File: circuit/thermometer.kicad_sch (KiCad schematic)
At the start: 1 part, among them IC1 ICL7107CPL

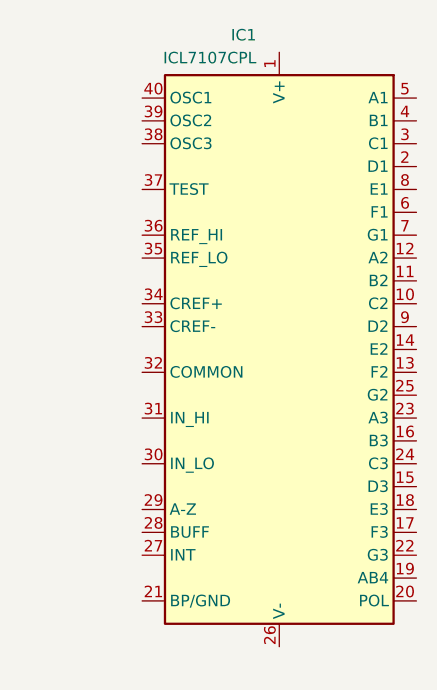
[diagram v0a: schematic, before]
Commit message: Configure oscillator
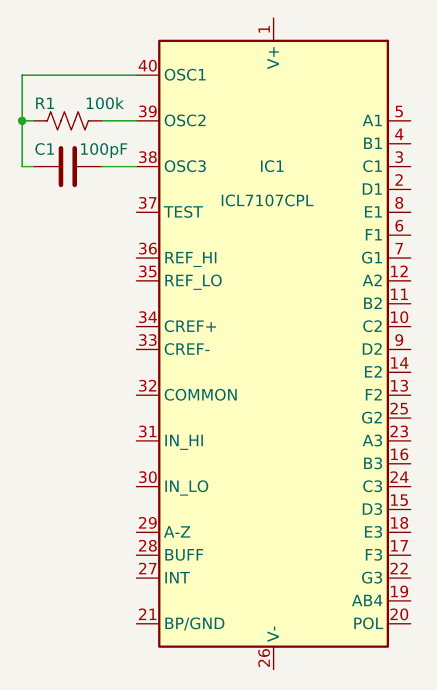
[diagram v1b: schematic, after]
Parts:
- added C1: 100pF, Capacitor_THT:C_Disc_D4.3mm_W1.9mm_P5.00mm, symbol Device:C
- added R1: 100k, Resistor_THT:R_Axial_DIN0207_L6.3mm_D2.5mm_P7.62mm_Horizontal, symbol Device:R_US
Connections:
- net at IC1.38 (OSC3): now also C1.1
- net at IC1.39 (OSC2): now also R1.1
- net at IC1.40 (OSC1): now also C1.2, R1.2
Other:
- moved on the sheet: IC1
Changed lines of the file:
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@@
 (kicad_sch (version 20230121) (generator eeschema)
   (paper "A4")
-  (symbol (lib_id "Analog_ADC:ICL7107CPL") (at 100.965 93.98 0) (mirror y) (unit 1)
+  (junction (at 72.39 68.58) (diameter 0) (color 0 0 0 0)
+  )
+  (wire (pts (xy 72.39 73.66) (xy 72.39 68.58))
+    (stroke (width 0) (type default))
+  )
+  (wire (pts (xy 72.39 68.58) (xy 72.39 63.5))
+    (stroke (width 0) (type default))
+  )
+  (wire (pts (xy 72.39 68.58) (xy 73.66 68.58))
+    (stroke (width 0) (type default))
+  )
+  (wire (pts (xy 72.39 63.5) (xy 85.09 63.5))
+    (stroke (width 0) (type default))
+  )
+  (wire (pts (xy 81.28 68.58) (xy 85.09 68.58))
+    (stroke (width 0) (type default))
+  )
+  (wire (pts (xy 81.28 73.66) (xy 85.09 73.66))
+    (stroke (width 0) (type default))
+  )
+  (wire (pts (xy 72.39 73.66) (xy 73.66 73.66))
+    (stroke (width 0) (type default))
+  )
+  (symbol (lib_id "Analog_ADC:ICL7107CPL") (at 100.33 96.52 0) (mirror y) (unit 1)
     (in_bom yes) (on_board yes) (dnp no)
-    (property "Reference" "IC1" (at 98.4232 59.055 0)
+    (property "Reference" "IC1" (at 101.6 73.66 0)
       (effects (font (size 1.27 1.27)) (justify left))
     )
-    (property "Value" "ICL7107CPL" (at 98.4232 61.595 0)
+    (property "Value" "ICL7107CPL" (at 104.775 77.47 0)
       (effects (font (size 1.27 1.27)) (justify left))
     )
-    (property "Footprint" "Package_DIP:DIP-40_W15.24mm" (at 100.965 125.73 0)
+    (property "Footprint" "Package_DIP:DIP-40_W15.24mm" (at 100.33 128.27 0)
       (effects (font (size 1.27 1.27)) hide)
     )
-    (property "Datasheet" "https://www.renesas.com/eu/en/www/doc/datasheet/icl7106-07-07s.pdf" (at 100.965 92.71 0)
+    (property "Datasheet" "https://www.renesas.com/eu/en/www/doc/datasheet/icl7106-07-07s.pdf" (at 100.33 95.25 0)
       (effects (font (size 1.27 1.27)) hide)
     )
@@
         )
       )
+    )
+  )
+  (symbol (lib_id "Device:R_US") (at 77.47 68.58 270) (unit 1)
+    (in_bom yes) (on_board yes) (dnp no)
+    (property "Reference" "R1" (at 74.93 66.675 90)
+      (effects (font (size 1.27 1.27)))
+    )
+    (property "Value" "100k" (at 79.375 66.675 90)
+      (effects (font (size 1.27 1.27)) (justify left))
+    )
+    (property "Footprint" "Resistor_THT:R_Axial_DIN0207_L6.3mm_D2.5mm_P7.62mm_Horizontal" (at 77.216 69.596 90)
+      (effects (font (size 1.27 1.27)) hide)
+    )
+    (property "Datasheet" "~" (at 77.47 68.58 0)
+      (effects (font (size 1.27 1.27)) hide)
+    )
+    (pin "1")
+    (pin "2")
+    (instances
+      (project "thermometer"
+        (path "/3d49da3f-611f-4a55-80ff-dd730f896849"
+          (reference "R1") (unit 1)
+        )
+      )
+    )
+  )
+  (symbol (lib_id "Device:C") (at 77.47 73.66 270) (unit 1)
+    (in_bom yes) (on_board yes) (dnp no)
+    (property "Reference" "C1" (at 74.93 71.755 90)
+      (effects (font (size 1.27 1.27)))
+    )
+    (property "Value" "100pF" (at 78.74 71.755 90)
+      (effects (font (size 1.27 1.27)) (justify left))
+    )
+    (property "Footprint" "Capacitor_THT:C_Disc_D4.3mm_W1.9mm_P5.00mm" (at 73.66 74.6252 0)
+      (effects (font (size 1.27 1.27)) hide)
+    )
+    (property "Datasheet" "~" (at 77.47 73.66 0)
+      (effects (font (size 1.27 1.27)) hide)
+    )
+    (pin "1")
+    (pin "2")
+    (instances
+      (project "thermometer"
+        (path "/3d49da3f-611f-4a55-80ff-dd730f896849"
+          (reference "C1") (unit 1)
+        )
+      )

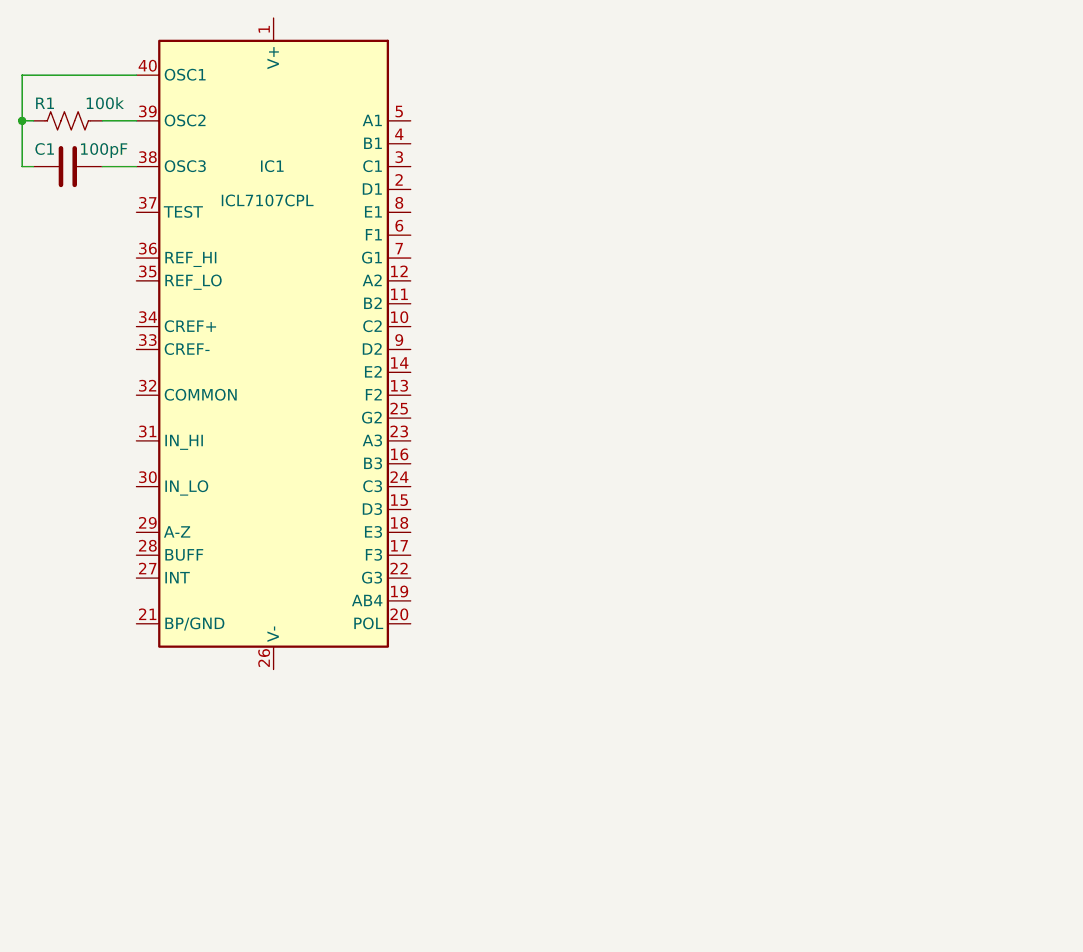
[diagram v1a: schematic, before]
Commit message: Add supporting components and power inverter
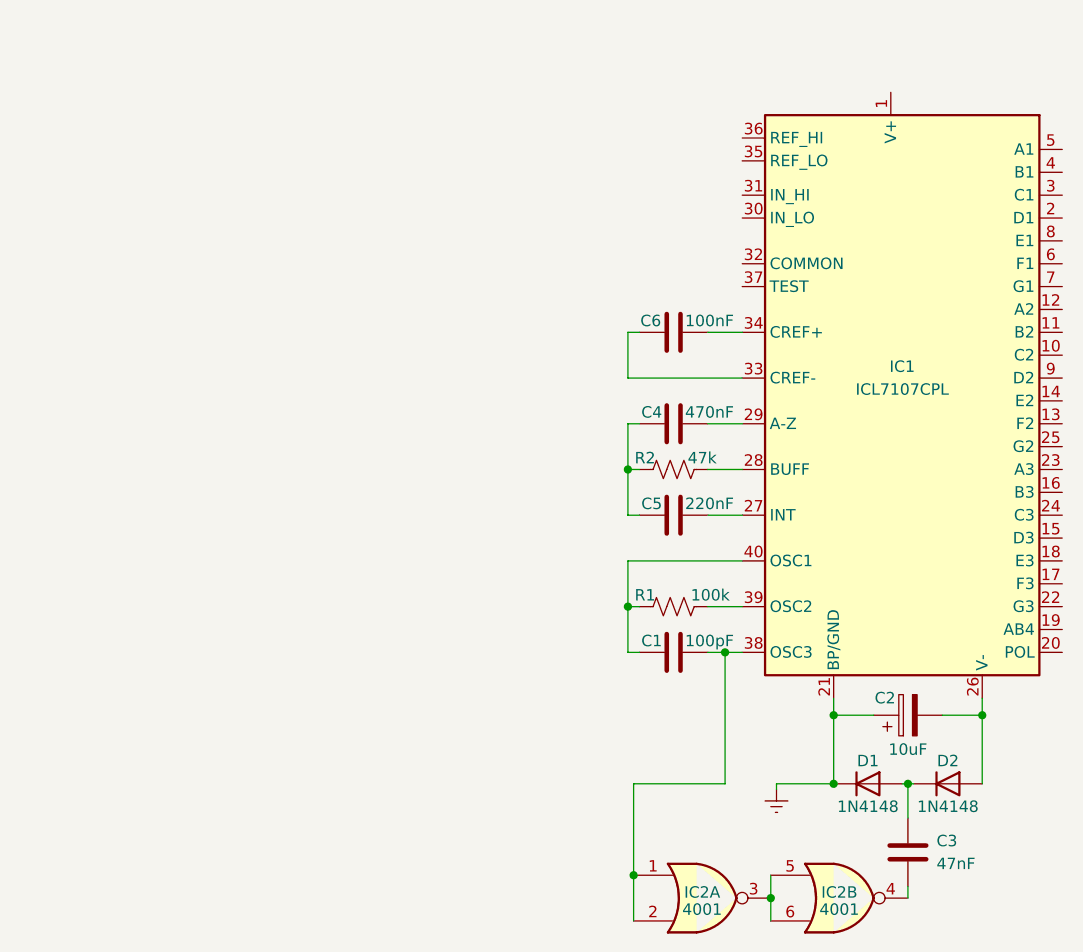
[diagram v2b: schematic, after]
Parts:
- added C2: 10uF, Capacitor_THT:CP_Radial_D5.0mm_P2.50mm, symbol Device:C_Polarized
- added C3: 47nF, Capacitor_THT:C_Disc_D4.3mm_W1.9mm_P5.00mm, symbol Device:C
- added C4: 470nF, Capacitor_THT:C_Disc_D4.3mm_W1.9mm_P5.00mm, symbol Device:C
- added C5: 220nF, Capacitor_THT:C_Disc_D4.3mm_W1.9mm_P5.00mm, symbol Device:C
- added C6: 100nF, symbol Device:C
- added D1, D2: 1N4148, Diode_THT:D_A-405_P7.62mm_Horizontal, symbol Device:D
- added IC2: 4001, Package_DIP:DIP-14_W7.62mm_Socket_LongPads, symbol 4xxx:4001
- added R2: 47k, Resistor_THT:R_Axial_DIN0207_L6.3mm_D2.5mm_P7.62mm_Horizontal, symbol Device:R_US
- IC1: footprint Package_DIP:DIP-40_W15.24mm -> Package_DIP:DIP-40_W15.24mm_Socket_LongPads
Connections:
- net Earth: now reaches IC1.21 (BP/GND)
- net Earth: now also C2.1, D1.1 (K)
- net at IC1.26 (V-): now also C2.2, D2.2 (A)
- net at IC1.27 (INT): now also C5.2
- net at IC1.28 (BUFF): now also R2.1
- net at IC1.29 (A-Z): now also C4.2
- net at IC1.33 (CREF-): now also C6.1
- net at IC1.34 (CREF+): now also C6.2
- net at C1.1, IC1.38 (OSC3): now also IC2.1, IC2.2
- new net: C4.1, C5.1, R2.2
- new net: C3.1, D1.2 (A), D2.1 (K)
- new net: C3.2, IC2.4
- new net: IC2.3, IC2.5, IC2.6
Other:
- moved on the sheet: C1, IC1, R1

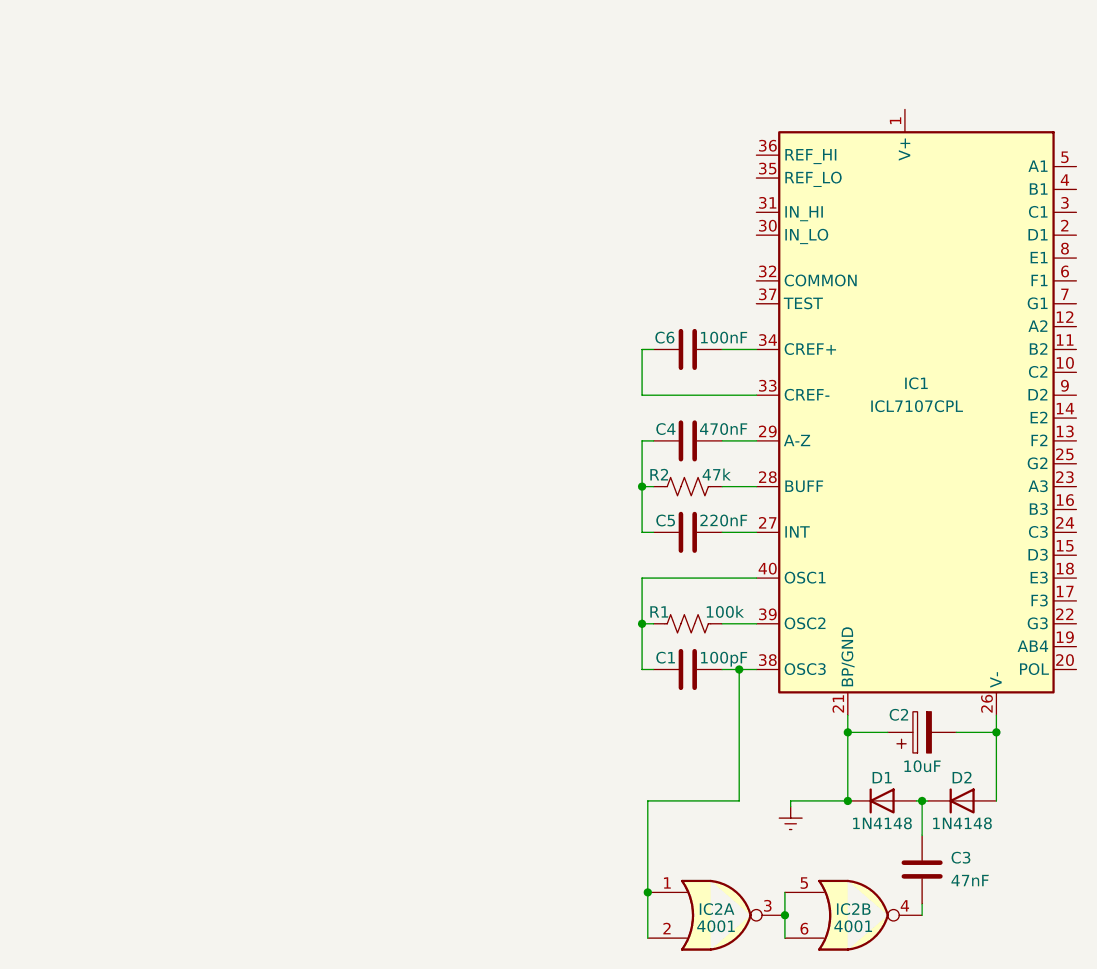
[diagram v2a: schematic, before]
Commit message: Place all remaining thermometer parts
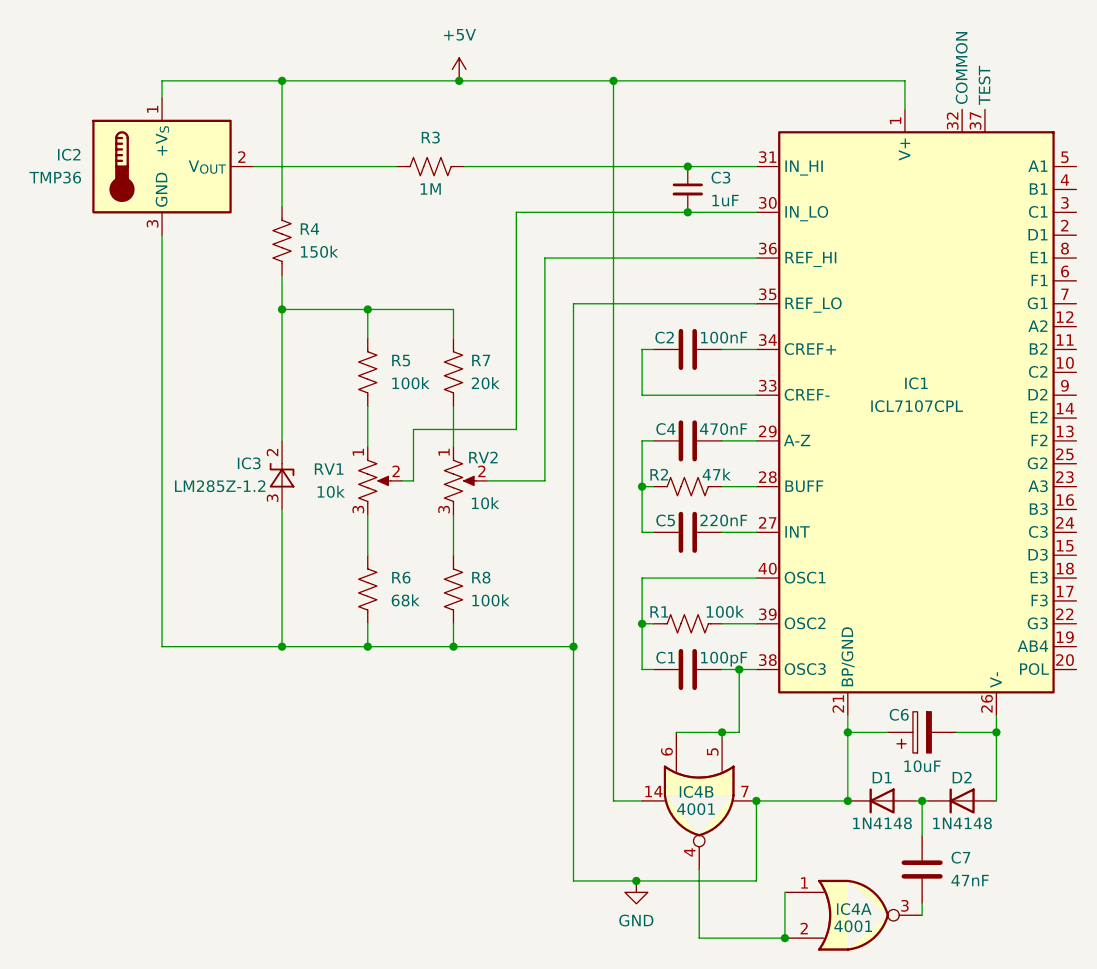
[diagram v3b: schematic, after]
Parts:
- added C3: 1uF, Capacitor_THT:C_Disc_D4.3mm_W1.9mm_P5.00mm, symbol Device:C_Small
- added IC2: TMP36, Package_TO_SOT_THT:TO-92_Inline, symbol Sensor_Temperature:LM35-LP
- added IC3: LM285Z-1.2, Package_TO_SOT_THT:TO-92_Inline, symbol Reference_Voltage:LM285Z-1.2
- added R3: 1M, Resistor_THT:R_Axial_DIN0204_L3.6mm_D1.6mm_P7.62mm_Horizontal, symbol Device:R_US
- added R4: 150k, Resistor_THT:R_Axial_DIN0204_L3.6mm_D1.6mm_P7.62mm_Horizontal, symbol Device:R_US
- added R5, R8: 100k, Resistor_THT:R_Axial_DIN0204_L3.6mm_D1.6mm_P7.62mm_Horizontal, symbol Device:R_US
- added R6: 68k, Resistor_THT:R_Axial_DIN0204_L3.6mm_D1.6mm_P7.62mm_Horizontal, symbol Device:R_US
- added R7: 20k, Resistor_THT:R_Axial_DIN0204_L3.6mm_D1.6mm_P7.62mm_Horizontal, symbol Device:R_US
- added RV1, RV2: 10k, Potentiometer_THT:Potentiometer_Piher_PT-6-V_Vertical, symbol Device:R_Potentiometer_US
- C2: renamed from C6; footprint (none) -> Capacitor_THT:C_Disc_D4.3mm_W1.9mm_P5.00mm
- C6: renamed from C2; footprint Capacitor_THT:CP_Radial_D5.0mm_P2.50mm -> Capacitor_THT:CP_Radial_Tantal_D4.5mm_P2.50mm
- D1, D2: footprint Diode_THT:D_A-405_P7.62mm_Horizontal -> Diode_THT:D_DO-34_SOD68_P7.62mm_Horizontal
- R1, R2: footprint Resistor_THT:R_Axial_DIN0207_L6.3mm_D2.5mm_P7.62mm_Horizontal -> Resistor_THT:R_Axial_DIN0204_L3.6mm_D1.6mm_P7.62mm_Horizontal
- renumbered C3 to C7, IC2 to IC4
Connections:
- net Earth is gone; now on net GND: C6.1, D1.1 (K), IC1.21 (BP/GND)
- net +5V: now reaches IC1.1 (V+)
- net +5V: now also IC4.14, IC2.1 (+V_{S}), R4.1
- net at IC1.30 (IN_LO): now also C3.2, RV1.2
- net at IC1.31 (IN_HI): now also C3.1, R3.2
- net GND: now reaches IC1.35 (REF_LO)
- net GND: now also IC4.7, IC2.3 (GND), IC3.3 (A), R6.2, R8.2
- net at IC1.36 (REF_HI): now also RV2.2
- net at C1.1, IC1.38 (OSC3): now also IC4.5, IC4.6; no longer IC4.1, IC4.2
- net at C7.2: now also IC4.3; no longer IC4.4
- new net: IC3.2 (K), R4.2, R5.1, R7.1
- new net: R5.2, RV1.1
- new net: IC2.2 (V_{OUT}), R3.1
- new net: R7.2, RV2.1
- new net: R8.1, RV2.3
- new net: IC4.1, IC4.2, IC4.4
- new net: R6.1, RV1.3
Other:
- moved on the sheet: IC1

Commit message: Place remaining parts
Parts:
- added DISP1: RS 587-967, Display_7Segment:7SegmentLED_LTS6760_LTS6780, symbol Display_Character:LTS-6960HR
- added DISP2: D512HDB, Display_7Segment:DA56-11SURKWA, symbol Display_Character:DA56-11EWA
- added DISP3: SA56-11HDB, Display_7Segment:7SegmentLED_LTS6760_LTS6780, symbol Display_Character:LTS-6960HR
- added J1: Conn_01x25_Socket, Connector_PinSocket_2.54mm:PinSocket_1x25_P2.54mm_Vertical, symbol Connector:Conn_01x25_Socket
- added J2: Conn_01x25_Pin, Connector_PinHeader_2.54mm:PinHeader_1x25_P2.54mm_Vertical, symbol Connector:Conn_01x25_Pin
- added R9: 620R, Resistor_THT:R_Axial_DIN0204_L3.6mm_D1.6mm_P7.62mm_Horizontal, symbol Device:R_US
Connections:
- net +5V: now also J1.1 (Pin_1)
- net GND: now also J1.25 (Pin_25)
- net at IC1.10 (C2): now also J1.10 (Pin_10)
- net at IC1.11 (B2): now also J1.11 (Pin_11)
- net at IC1.12 (A2): now also J1.12 (Pin_12)
- net at IC1.13 (F2): now also J1.13 (Pin_13)
- net at IC1.14 (E2): now also J1.14 (Pin_14)
- net at IC1.15 (D3): now also J1.15 (Pin_15)
- net at IC1.16 (B3): now also J1.16 (Pin_16)
- net at IC1.17 (F3): now also J1.17 (Pin_17)
- net at IC1.18 (E3): now also J1.18 (Pin_18)
- net at IC1.19 (AB4): now also J1.19 (Pin_19)
- net at IC1.2 (D1): now also J1.2 (Pin_2)
- net at IC1.20 (POL): now also J1.20 (Pin_20)
- net at IC1.22 (G3): now also J1.24 (Pin_24)
- net at IC1.23 (A3): now also J1.23 (Pin_23)
- net at IC1.24 (C3): now also J1.22 (Pin_22)
- net at IC1.25 (G2): now also J1.21 (Pin_21)
- net at IC1.3 (C1): now also J1.3 (Pin_3)
- net at IC1.4 (B1): now also J1.4 (Pin_4)
- net at IC1.5 (A1): now also J1.5 (Pin_5)
- net at IC1.6 (F1): now also J1.6 (Pin_6)
- net at IC1.7 (G1): now also J1.7 (Pin_7)
- net at IC1.8 (E1): now also J1.8 (Pin_8)
- net at IC1.9 (D2): now also J1.9 (Pin_9)
- new net: DISP2.9 (dp2), R9.1
- new net: J2.25 (Pin_25), R9.2
- new net: DISP1.7 (CA1), DISP1.8 (CA±), DISP2.13 (ca2), DISP2.14 (ca1), DISP3.8 (C.A.), J2.1 (Pin_1)
- new net: DISP2.8 (c2), J2.10 (Pin_10)
- new net: DISP2.10 (b2), J2.11 (Pin_11)
- new net: DISP2.11 (a2), J2.12 (Pin_12)
- new net: DISP2.12 (f2), J2.13 (Pin_13)
- new net: DISP2.5 (e2), J2.14 (Pin_14)
- new net: DISP2.2 (d1), J2.15 (Pin_15)
- new net: DISP2.15 (b1), J2.16 (Pin_16)
- new net: DISP2.18 (f1), J2.17 (Pin_17)
- new net: DISP2.1 (e1), J2.18 (Pin_18)
- new net: DISP1.3 (b), DISP1.6 (a), J2.19 (Pin_19)
- new net: DISP3.2 (d), J2.2 (Pin_2)
- new net: DISP1.1 (-), J2.20 (Pin_20)
- new net: DISP2.7 (g2), J2.21 (Pin_21)
- new net: DISP2.3 (c1), J2.22 (Pin_22)
- new net: DISP2.16 (a1), J2.23 (Pin_23)
- new net: DISP2.17 (g1), J2.24 (Pin_24)
- new net: DISP3.4 (c), J2.3 (Pin_3)
- new net: DISP3.6 (b), J2.4 (Pin_4)
- new net: DISP3.7 (a), J2.5 (Pin_5)
- new net: DISP3.9 (f), J2.6 (Pin_6)
- new net: DISP3.10 (g), J2.7 (Pin_7)
- new net: DISP3.1 (e), J2.8 (Pin_8)
- new net: DISP2.6 (d2), J2.9 (Pin_9)
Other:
- moved on the sheet: C1, C2, C3, C4, C5, C6, C7, D1, D2, IC1, IC2, IC3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
